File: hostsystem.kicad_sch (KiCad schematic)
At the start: 93 parts, among them J1001 Conn_01x06_Pin, J1002 TC2050, J1003 Conn_01x03_Pin, J1004 Conn_01x06_Pin, U1001 LMK1C1102PWR, U1002 AM6231ASGGGAALW, U1003 SN74LVC2G241DCUR, U1004 AT24C32D-STUM-T, X1001 ECS-2520MV-250-CN-TR, X1002 25MHz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

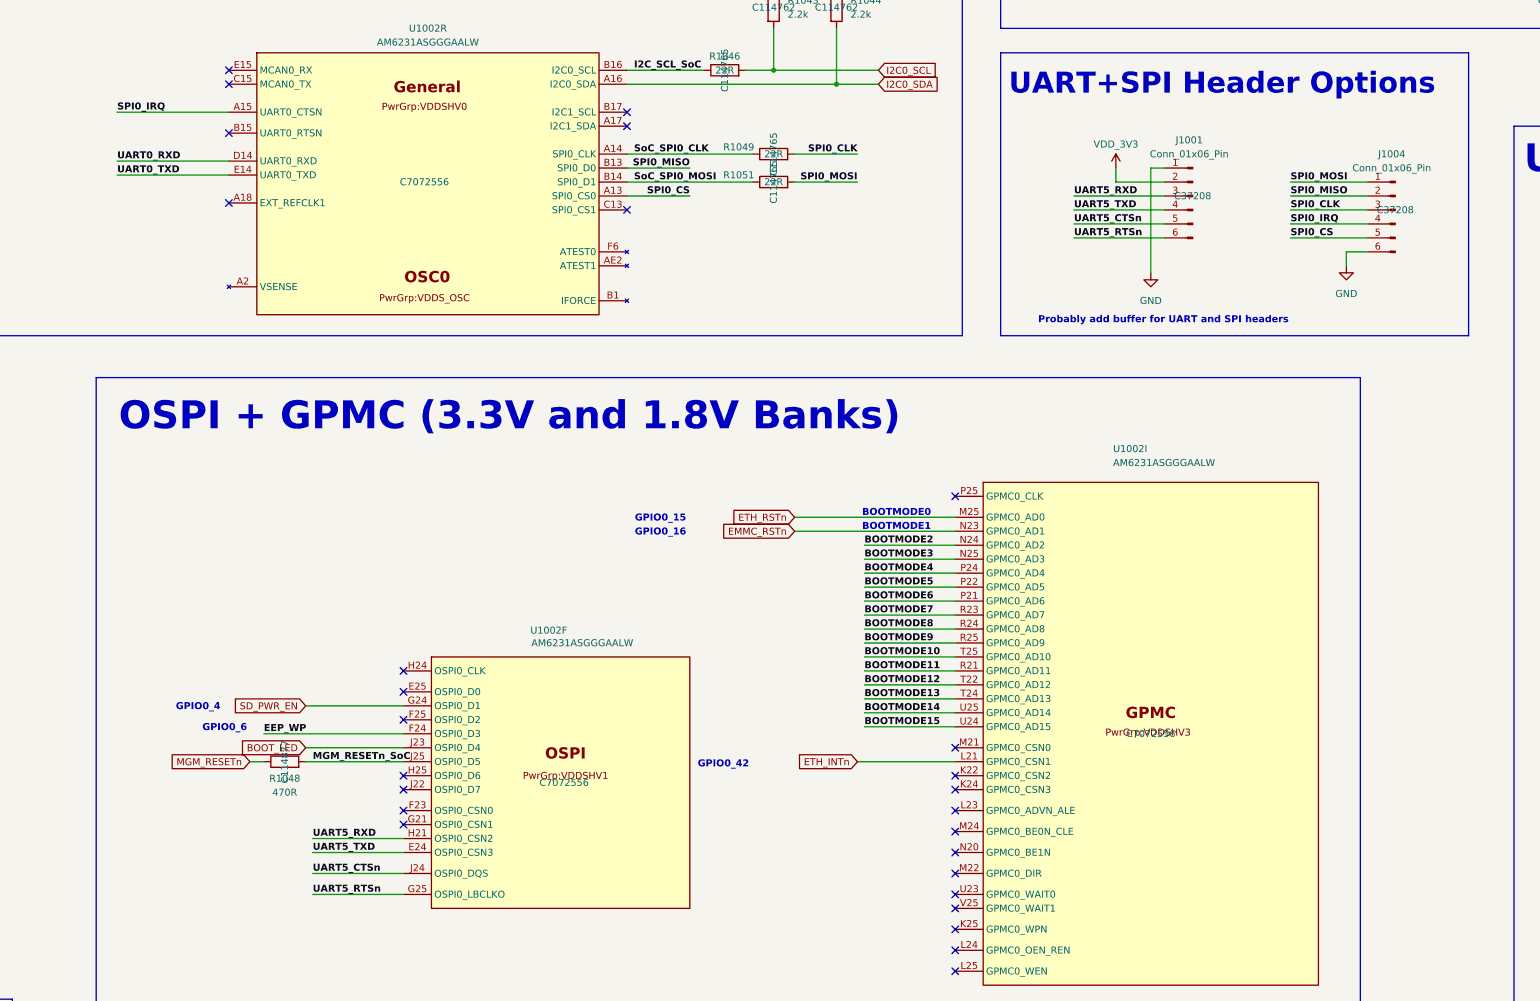
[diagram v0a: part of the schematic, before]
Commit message: Fixed MGM240P pinout, replaced 01x06 SPI and UART header pins with 02x06 header pins that will be connected via jumper shunts, deleted MMC1 (microSD)
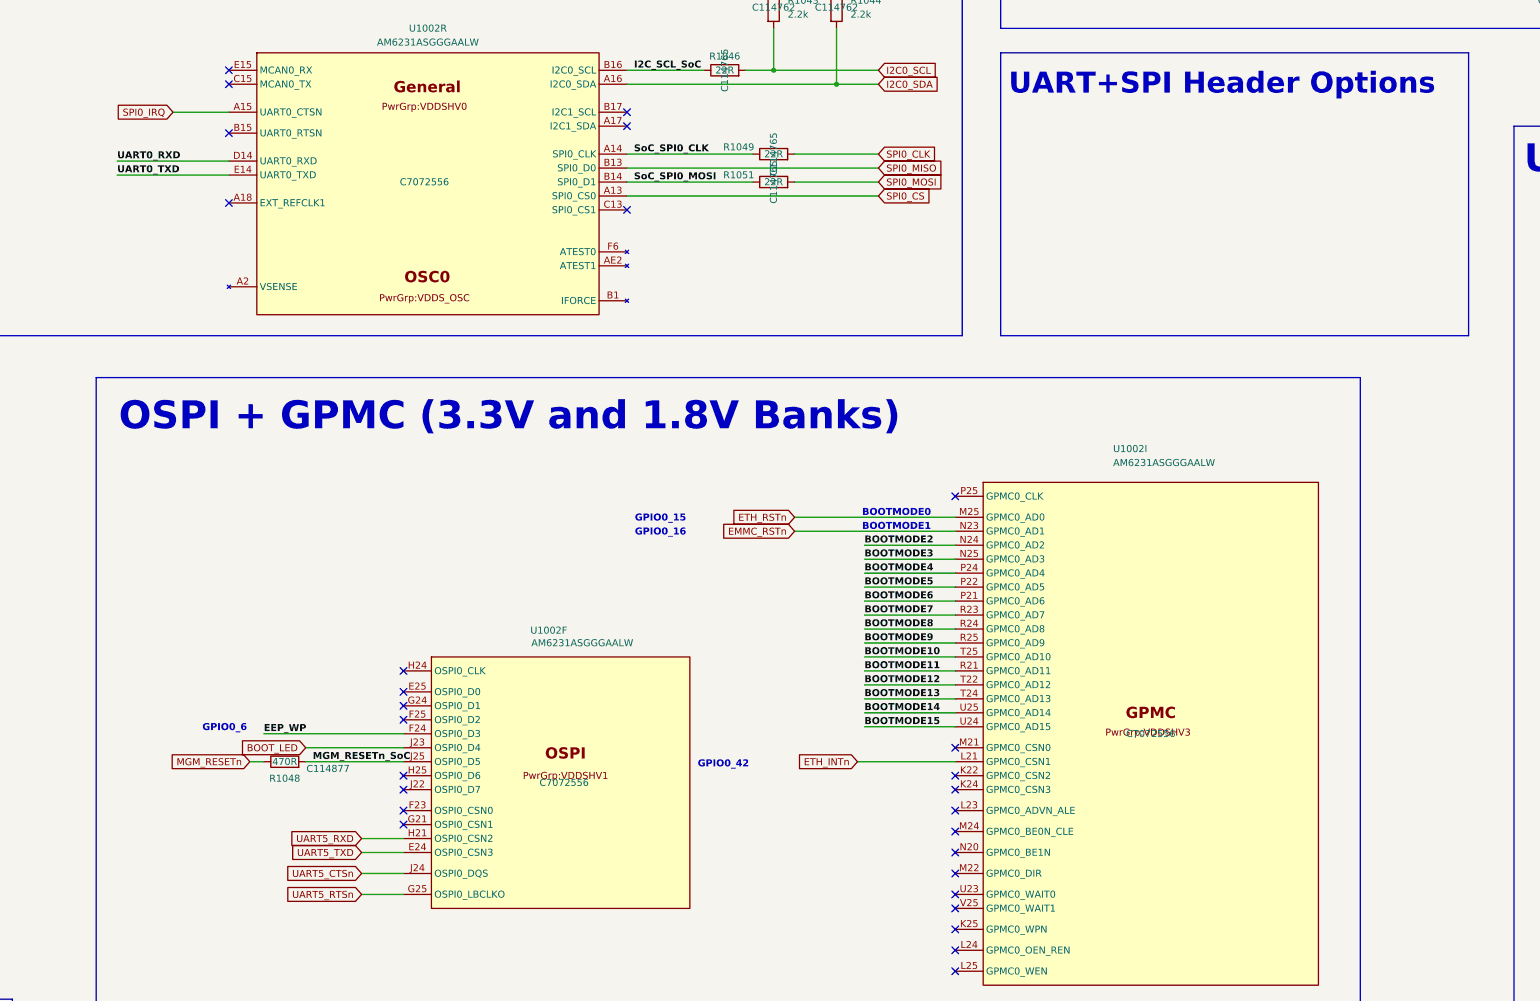
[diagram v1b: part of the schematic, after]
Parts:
- removed J1001, J1004: Conn_01x06_Pin, Connector_PinHeader_2.54mm:PinHeader_1x06_P2.54mm_Vertical, symbol Connector:Conn_01x06_Pin
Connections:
- net SD_PWR_EN: no longer names the net of U1002.G24 (OSPI0_D1)
- no-connect marks 108 -> 109
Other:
- note removed: "GPIO0_4"
- note removed: "Probably add buffer for UART and SPI headers"
